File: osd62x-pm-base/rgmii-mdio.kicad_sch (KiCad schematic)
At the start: 0 parts

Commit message: Symbol unit E started and placed
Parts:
- added U2: ~, symbol octavo_Library:osd62x-pm

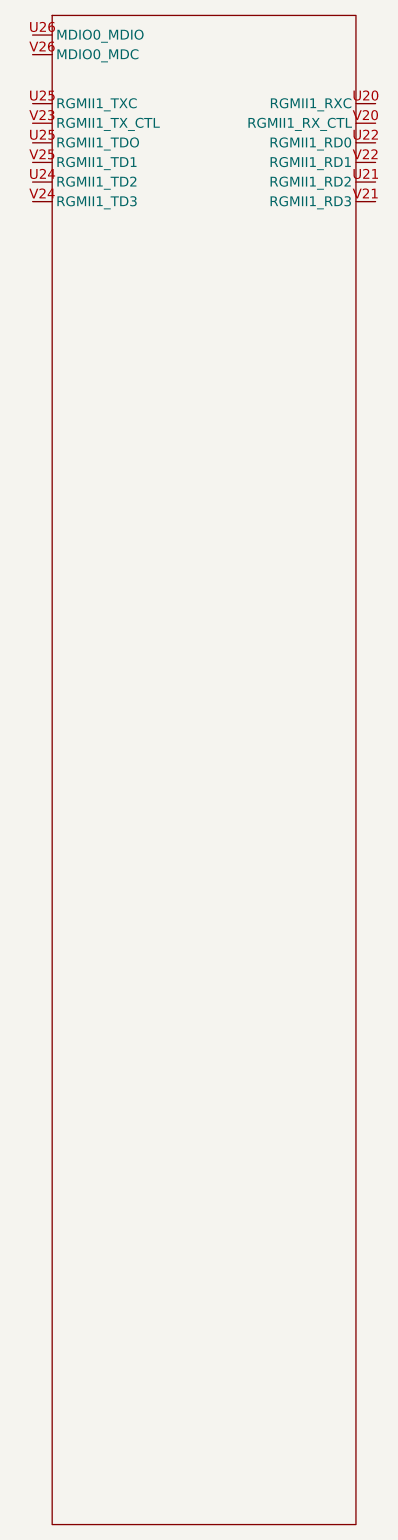
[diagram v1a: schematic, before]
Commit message: Symbol unit E completed
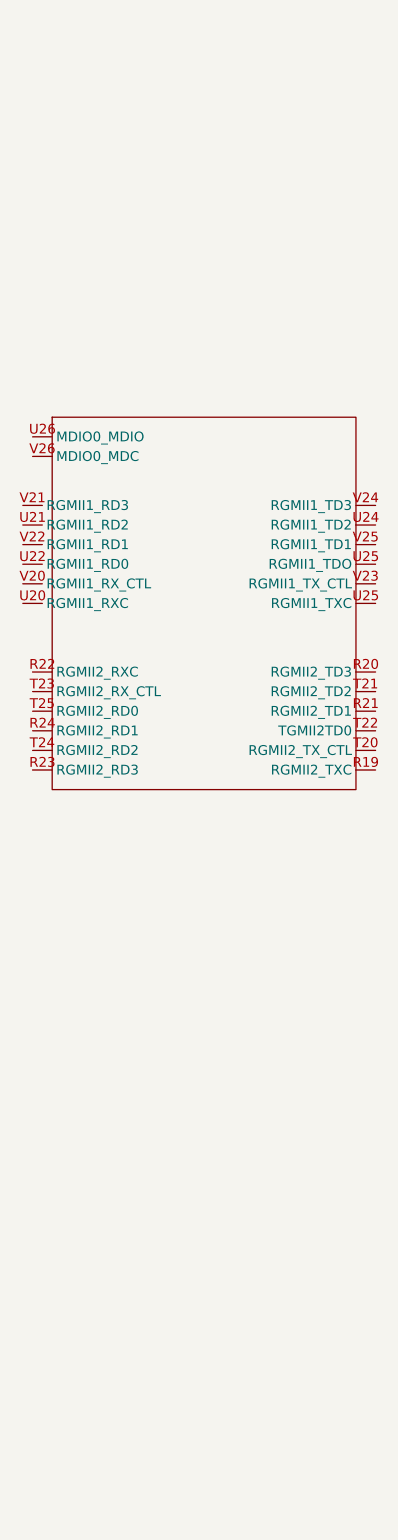
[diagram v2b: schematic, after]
